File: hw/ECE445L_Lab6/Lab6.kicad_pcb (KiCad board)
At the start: 2 copper layers, 101.6 x 61 mm, 36 parts, among them J1 JST1.25, J3 Speaker, J4 Debugger, J5 ZX62D-B-5PA8_30_, J6 Header2, J7 Testpoints, SW1 RST, SW2 Mode, SW3 Mode, SW4 Mode, SW5 Mode, U1 Adafruit ST7735R, U2 LP2950-33LPRE3, U3 M0G3507QDGS32RQ1, Y1 16MHz

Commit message: updates thus far
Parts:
- moved Y1 16.0 mm to (103.7, 64.0)
- moved U3 11.1 mm to (113.7, 73.8)
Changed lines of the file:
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@@
 	(footprint "ECE445L:ABM3"
 		(layer "F.Cu")
-		(at 119.680681 64.002049 180)
+		(at 103.65 64.002049 180)
 		(descr "ABM3")
 		(tags "Crystal or Oscillator")
@@
 	(footprint "ECE445L:VSSOP_0.5mm_32pin_handsolder"
 		(layer "F.Cu")
-		(at 124.46 71.12 -90)
+		(at 113.72 73.825 -90)
 		(descr "VSSOP 0.5mm 32 pins")
 		(tags "VSSOP SO")

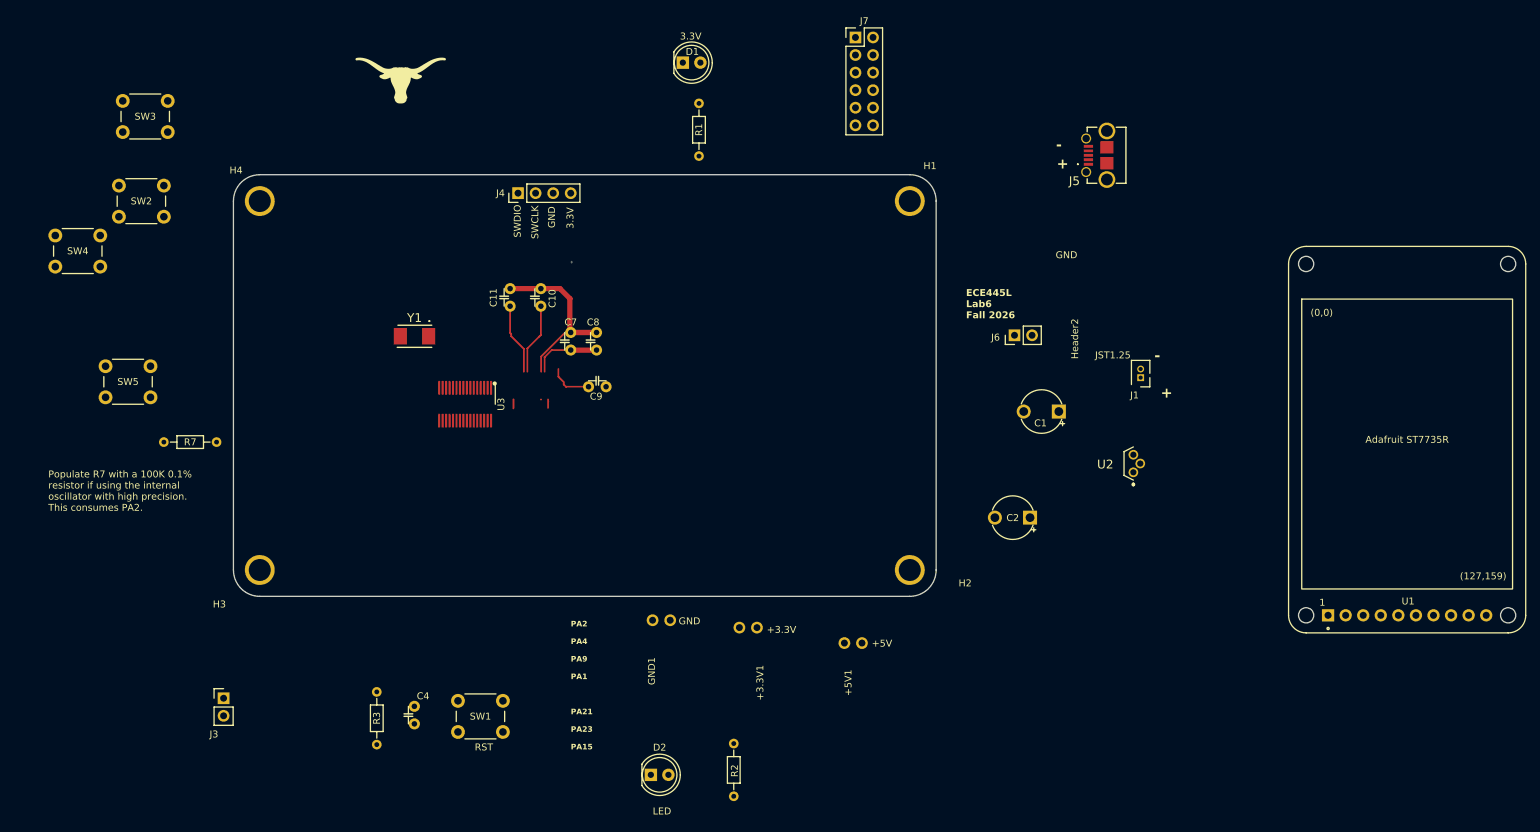
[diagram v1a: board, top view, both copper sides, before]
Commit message: linking errors ignored and zero errors in pcb
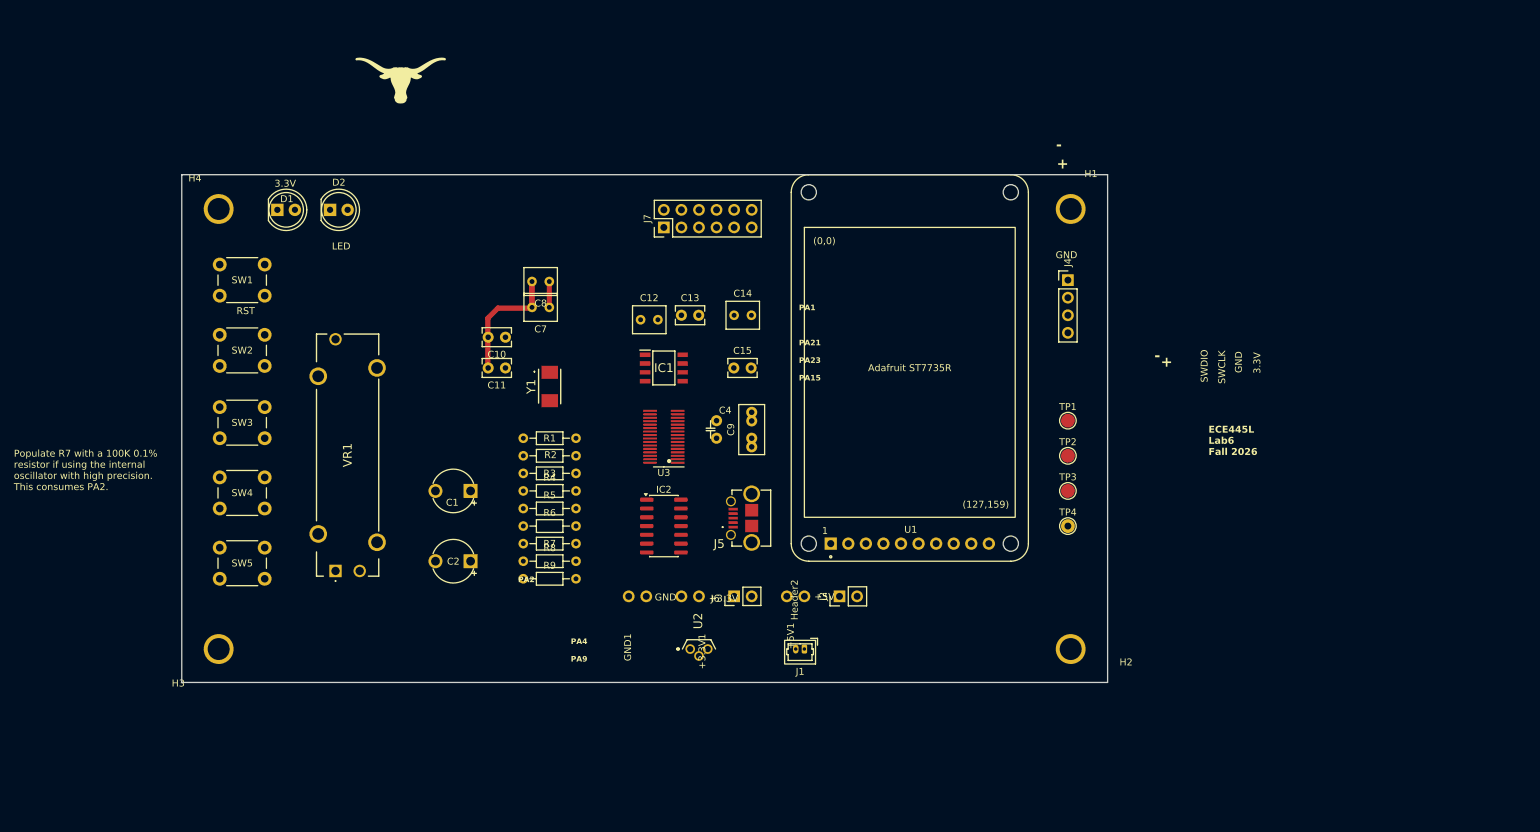
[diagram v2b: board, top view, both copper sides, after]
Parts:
- removed J3: Speaker, Connector_PinHeader_2.54mm:PinHeader_1x02_P2.54mm_Vertical
- added C12: 0.1uF, Capacitor_THT:C_Rect_L4.6mm_W3.8mm_P2.50mm_MKS02_FKP02, F.Cu at (136.3, 61.6)
- added C13: 1uF, Capacitor_THT:C_Rect_L4.0mm_W2.5mm_P2.50mm, F.Cu at (142.2, 61.0)
- added C14: 0.1uF, Capacitor_THT:C_Rect_L4.6mm_W3.8mm_P2.50mm_MKS02_FKP02, F.Cu at (149.9, 61.0)
- added C15: 1uF, Capacitor_THT:C_Rect_L4.0mm_W2.5mm_P2.50mm, F.Cu at (149.8, 68.6)
- added IC1: AD8300ARZ, ECE445L:SOIC127P600X175-8N, F.Cu at (139.7, 68.6)
- added IC2: AD8604WARZ, Package_SO:SOIC-14_3.9x8.7mm_P1.27mm, F.Cu at (139.7, 91.4)
- added J2: Conn_01x02, Connector_PinHeader_2.54mm:PinHeader_1x02_P2.54mm_Vertical, F.Cu at (165.1, 101.6)
- added R4: 10k, ECE445L:R_Axial_DIN0204_L3.6mm_D1.6mm_P7.62mm_Horizontal, F.Cu at (119.4, 86.4)
- added R5: 10k, ECE445L:R_Axial_DIN0204_L3.6mm_D1.6mm_P7.62mm_Horizontal, F.Cu at (119.4, 88.9)
- added R6: 10k, ECE445L:R_Axial_DIN0204_L3.6mm_D1.6mm_P7.62mm_Horizontal, F.Cu at (119.4, 91.4)
- added R8: 10k, ECE445L:R_Axial_DIN0204_L3.6mm_D1.6mm_P7.62mm_Horizontal, F.Cu at (119.4, 96.5)
- added R9: 10k, ECE445L:R_Axial_DIN0204_L3.6mm_D1.6mm_P7.62mm_Horizontal, F.Cu at (119.4, 99.1)
- added TP1: ADC_IN, TestPoint:TestPoint_Pad_D2.0mm, F.Cu at (198.1, 76.2)
- added TP2: ANALOG_OUT, TestPoint:TestPoint_Pad_D2.0mm, F.Cu at (198.1, 81.3)
- added TP3: DAC_RAW, TestPoint:TestPoint_Pad_D2.0mm, F.Cu at (198.1, 86.4)
- added TP4: TP_BATT, TestPoint:TestPoint_THTPad_D2.0mm_Drill1.0mm, F.Cu at (198.1, 91.4)
- added VR1: PTA2043-2015CPB103, ECE445L:PTA20432015CPB103, F.Cu at (92.2, 97.9)
- C10, C11: footprint ECE445L:C_Radial_100mil -> Capacitor_THT:C_Rect_L4.0mm_W2.5mm_P2.50mm
- C7, C8: footprint ECE445L:C_Radial_100mil -> Capacitor_THT:C_Rect_L4.6mm_W3.8mm_P2.50mm_MKS02_FKP02
- C9: footprint ECE445L:C_Radial_100mil -> Capacitor_THT:C_Rect_L7.0mm_W3.5mm_P2.50mm_P5.00mm
- J1: footprint ECE445L:JST-1x02_1.25mm -> Connector_Molex:Molex_PicoBlade_53047-0210_1x02_P1.25mm_Vertical
- U3: footprint ECE445L:VSSOP_0.5mm_32pin_handsolder -> ECE445L:generic_VSSOP_0.5mm
- moved D2 93.9 mm to (91.4, 45.7)
- moved C1 85.8 mm to (111.8, 86.4)
- moved C2 81.1 mm to (111.8, 96.5)
- moved J4 80.5 mm to (198.1, 55.9), turned to 0 degrees
- moved J5 73.4 mm to (152.3, 90.3)
- moved U1 72.7 mm to (175.3, 68.6)
- moved SW1 71.9 mm to (75.5, 53.6)
- moved U2 69.0 mm to (143.5, 109.2), turned to 0 degrees
- moved J1 62.5 mm to (160.0, 109.2)
- moved D1 62.4 mm to (83.8, 45.7)
- moved C4 60.1 mm to (147.3, 78.7)
- moved J6 55.4 mm to (149.9, 101.6)
- moved R1 54.7 mm to (119.4, 78.7), turned to 0 degrees
- moved R2 54.3 mm to (127.0, 81.3), turned to 180 degrees
- moved R7 54.0 mm to (119.4, 94.0)
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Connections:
- net Net-(J1-Pin_1) renamed /Batt
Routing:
- net PA6/HFXOUT: track 10.3 -> 0.00 mm
- net PA5/HFXIN: track 10.3 -> 0.00 mm
- net GND: track 30.0 -> 21.9 mm
- net +3V3: track 10.1 -> 3.73 mm
- net Net-(U3-VCORE): track 6.26 -> 0.00 mm
- net SWCLK: track 1.33 -> 0.00 mm
- net PA10: track 1.32 -> 0.00 mm
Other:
- board size 101.6 x 61 mm -> 133.9 x 73.4 mm

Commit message: routing finished i think
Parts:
- moved C14 38.8 mm to (129.6, 94.0)
- moved R5 29.0 mm to (105.4, 63.5)
- moved R7 29.0 mm to (105.4, 68.6)
- moved R9 29.0 mm to (105.4, 73.7)
- moved R2 29.0 mm to (113.0, 55.9)
- moved R4 29.0 mm to (105.4, 61.0)
- moved R1 29.0 mm to (105.4, 53.3)
- moved R3 29.0 mm to (113.0, 58.4)
- moved R6 29.0 mm to (105.4, 66.0)
- moved R8 29.0 mm to (105.4, 71.1)
- moved C15 28.7 mm to (129.6, 88.9)
- moved C4 23.4 mm to (152.4, 55.9), turned to 180 degrees
- moved C7 22.0 mm to (144.8, 55.9)
- moved U3 19.3 mm to (147.3, 63.5), turned to -90 degrees
- moved C13 18.3 mm to (132.1, 76.2), turned to 180 degrees
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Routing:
- net GND: track 21.9 -> 401.4 mm, vias 0 -> 1
- net +3V3: track 3.73 -> 321.9 mm
- net PA22: track 0.00 -> 123.6 mm, vias 0 -> 2
- net PA8/SPI0_CS0: track 0.00 -> 97.1 mm, vias 0 -> 2
- net Net-(U3-NRST): track 0.00 -> 95.8 mm, vias 0 -> 1
- net PA3: track 0.00 -> 87.5 mm, vias 0 -> 2
- net PA26: track 0.00 -> 85.1 mm
- net /DAC_RAW: track 0.00 -> 84.6 mm, vias 0 -> 2
- net /ANALOG_OUT: track 0.00 -> 83.4 mm, vias 0 -> 1
- net PA2: track 0.00 -> 81.4 mm, vias 0 -> 2
- net /Batt: track 0.00 -> 75.1 mm
- net PA23: track 0.00 -> 75.0 mm, vias 0 -> 4
- net PA10: track 0.00 -> 74.5 mm, vias 0 -> 2
- net PA9: track 0.00 -> 71.2 mm, vias 0 -> 2
- net PA7: track 0.00 -> 69.4 mm
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
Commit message: complete lab
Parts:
- C9: footprint Capacitor_THT:C_Rect_L7.0mm_W3.5mm_P2.50mm_P5.00mm -> Capacitor_THT:C_Rect_L4.6mm_W3.8mm_P2.50mm_MKS02_FKP02
- moved R5 58.2 mm to (154.9, 94.0), turned to 90 degrees
- moved R6 51.2 mm to (149.9, 91.4), turned to 180 degrees
- moved J7 36.1 mm to (111.8, 71.1), turned to 180 degrees
- moved C13 30.6 mm to (152.4, 53.3)
- moved J5 30.5 mm to (176.2, 109.3), turned to 180 degrees
- moved Y1 28.5 mm to (134.1, 84.7)
- moved C11 28.2 mm to (128.0, 81.3), turned to -90 degrees
- moved C10 26.1 mm to (128.0, 88.9), turned to 90 degrees
- moved R4 24.4 mm to (124.5, 45.7)
- moved R7 24.3 mm to (121.9, 86.4), turned to 90 degrees
- moved C9 23.3 mm to (132.1, 68.6), turned to 180 degrees
- moved C15 21.7 mm to (137.2, 68.5), turned to 90 degrees
- moved C12 20.5 mm to (142.2, 53.3)
- moved TP4 19.3 mm to (190.5, 109.2)
- moved U3 18.0 mm to (134.6, 76.2)
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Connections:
- C9 pad 1: Net-(U3-VCORE) -> GND
- C9 pad 2: GND -> Net-(U3-VCORE)
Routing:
- net +3V3: track 321.9 -> 400.1 mm, vias 0 -> 3
- net PA2: track 81.4 -> 40.8 mm, vias 2 -> 0
- net PA21: track 67.5 -> 32.0 mm
- net PA11/SPI0_SCK: track 40.7 -> 70.9 mm, vias 2 -> 1
- net PA12: track 46.6 -> 17.1 mm
- net Net-(U3-VCORE): track 37.1 -> 8.36 mm, vias 2 -> 1
- net PA14/SPI0_PICO: track 34.3 -> 63.0 mm
- net PA3: track 87.5 -> 66.7 mm, vias 2 -> 1
- net PA1: track 16.4 -> 36.3 mm, vias 0 -> 2
- net PA13/TFT_D/C: track 45.6 -> 65.2 mm, vias 1 -> 0
- net PA10: track 74.5 -> 55.2 mm, vias 2 -> 0
- net PA25/SPI1_CS3: track 39.9 -> 59.0 mm
- net SWDIO: track 62.7 -> 81.4 mm
- net PA26: track 85.1 -> 68.4 mm, vias 0 -> 1
- net PA17/SPI1_CLK: track 54.4 -> 70.4 mm, vias 1 -> 3
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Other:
- board text added: "ECE445L Lab6 Fall 2026 Tanai Prathapam tsp824"
- board text removed: "ECE445L Lab6 Fall 2026"
